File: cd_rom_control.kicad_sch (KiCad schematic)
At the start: 74 parts, among them IC103 CXD1167Q, IC104 D78C14GF, IC105 D6378GF, IC106 D4364G, P401 Conn_01x10, P404 Conn_01x08, P7 Conn_01x07, Q1 Q_NPN_CBE, Q102 Q_NPN_CBE, Q203 15 29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

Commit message: More passives on back.
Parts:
- added C138 (x5): ?, A-PCENGINE:SMD_0805_Narrow_Long, symbol Device:C
- added C138: ?, A-PCENGINE:SMD_0805_Narrow, symbol Device:C
- added R105: ?, A-PCENGINE:SMD_0805_Narrow, symbol Device:R
- added R105 (x19): ?, A-PCENGINE:SMD_0805_Narrow_Long, symbol Device:R
- added TP1 (x6), TP7 (x6): ~, A-PCENGINE:Test_Point_1.5mm, symbol Connector:TestPoint
- renumbered Q1 to Q105
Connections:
- net +5VD: now also C138.1, C138.1, C138.1, C138.1, C138.2, C138.2, TP1.1
- net ATSC: now also TP7.1
- net BCLK: now also R105.2
- net CIF4: now also R105.2
- net CIF5: now also R105.2
- net CIF6: now also R105.2
- net DA13: now also R105.1
- net DA14: now also R105.1
- net DA15: now also R105.1, R105.1
- net DA7: now also R105.1
- net DA8: now also R105.2
- net DATA: now also R105.2
- net FE: now also TP7.1
- net GND: now also C138.1, C138.1, C138.2, C138.2, C138.2, C138.2, R105.1, R105.1, R105.2
- net LRCK: now also R105.2
- net MD2: now also R105.2
- net P404P6: now also R105.2, R105.2
- net P7P5: now also TP7.1
- net P7P6: now also TP7.1
- net SCOR: now also R105.1
- net X0: now also R105.2
- net X1: now also R105.2, TP1.1
- net X2: now also R105.2
- net X3: now also R105.2, TP1.1
- net X4: now also R105.2
- net X5: now also R105.2, TP1.1
- net X6: now also R105.2, TP1.1
- net X7: now also R105.2, TP1.1
- net XCLK: now also TP7.1
- net at P3.1 (Pin_1): now also R105.1, TP7.1
- net at IC104.49: now also R105.1
- net at IC104.50: now also R105.1
- net at IC104.51: now also R105.1
- net at IC104.52: now also R105.1
- net at IC104.53: now also R105.1
- net at IC104.54: now also R105.1
- net at IC104.55: now also R105.1
- net at IC104.56: now also R105.1
- net at IC103.22 (SBSO): now also R105.1
- net at IC103.79 (WDCK): now also R105.2
- net at IC103.80 (LRCK): now also R105.1
- new net WCLK: R105.1
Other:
- moved on the sheet: C138, C951, P3, P401, P404, P7, Q102, R105, RA502

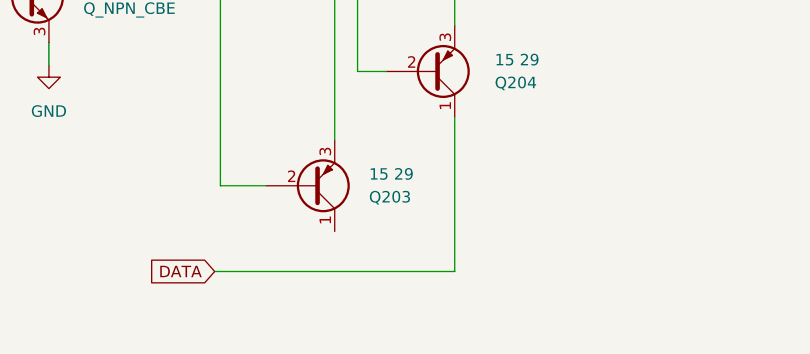
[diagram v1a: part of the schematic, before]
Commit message: Yet more passives on back.
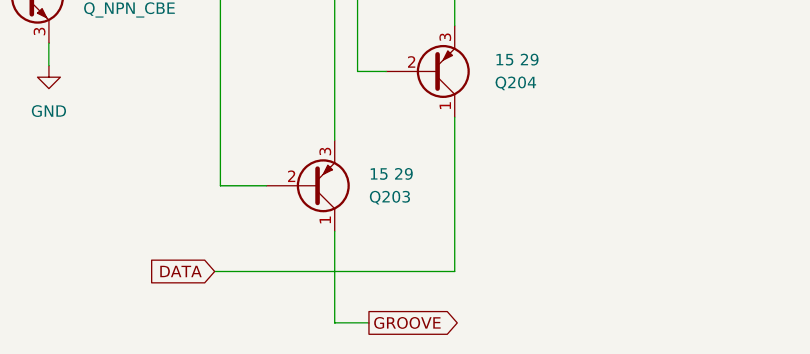
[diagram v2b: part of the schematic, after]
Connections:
- net GROOVE: now reaches Q203.1 (C)
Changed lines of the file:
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@@
+    (stroke (width 0) (type default))
+  )
+  (wire (pts (xy -20.32 314.96) (xy -20.32 325.12))
     (stroke (width 0) (type default))
   )
@@
   )
   (wire (pts (xy 220.98 269.24) (xy 220.98 273.685))
+    (stroke (width 0) (type default))
+  )
+  (wire (pts (xy -20.32 325.12) (xy -16.51 325.12))
     (stroke (width 0) (type default))
   )
@@
       (effects (font (size 1.27 1.27)) (justify left) hide)
     )
+  )
+  (global_label "GROOVE" (shape output) (at -16.51 325.12 0) (fields_autoplaced)
+    (effects (font (size 1.27 1.27)) (justify left))
+    (property "Intersheetrefs" "${INTERSHEET_REFS}" (at -6.0862 325.12 0)
+      (effects (font (size 1.27 1.27)) (justify left) hide)
+    )

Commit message: Fix DRC errors.
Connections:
- net DATA: no longer Q204.1 (C), R105.2
- net BW: now reaches Q102.1 (C), R105.2
- new net DATA2: Q204.1 (C), R105.2
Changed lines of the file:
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@@
   (junction (at -104.14 262.89) (diameter 0) (color 0 0 0 0)
   )
+  (junction (at 106.68 -31.115) (diameter 0) (color 0 0 0 0)
+  )
   (junction (at 121.285 29.845) (diameter 0) (color 0 0 0 0)
   )
@@
     (stroke (width 0) (type default))
   )
-  (wire (pts (xy -6.985 319.405) (xy -6.985 302.26))
+  (wire (pts (xy -6.985 307.848) (xy -6.985 302.26))
     (stroke (width 0) (type default))
   )
@@
     (stroke (width 0) (type default))
   )
+  (wire (pts (xy 106.68 -31.115) (xy 113.03 -31.115))
+    (stroke (width 0) (type default))
+  )
   (wire (pts (xy -44.45 220.98) (xy -114.3 220.98))
     (stroke (width 0) (type default))
@@
     (stroke (width 0) (type default))
   )
-  (wire (pts (xy -33.655 319.405) (xy -6.985 319.405))
+  (wire (pts (xy 0 307.848) (xy -6.985 307.848))
     (stroke (width 0) (type default))
   )
@@
     )
   )
-  (global_label "DATA" (shape input) (at 206.375 34.29 90) (fields_autoplaced)
+  (global_label "DATA2" (shape input) (at 206.375 34.29 90) (fields_autoplaced)
     (effects (font (size 1.27 1.27)) (justify left))
-    (property "Intersheetrefs" "${INTERSHEET_REFS}" (at 206.375 26.89 90)
+    (property "Intersheetrefs" "${INTERSHEET_REFS}" (at 206.375 25.6805 90)
       (effects (font (size 1.27 1.27)) (justify left) hide)
     )
@@
     )
   )
+  (global_label "BW" (shape input) (at 113.03 -31.115 0) (fields_autoplaced)
+    (effects (font (size 1.27 1.27)) (justify left))
+    (property "Intersheetrefs" "${INTERSHEET_REFS}" (at 118.7366 -31.115 0)
+      (effects (font (size 1.27 1.27)) (justify left) hide)
+    )
+  )
   (global_label "SCOR" (shape output) (at 121.285 21.59 90) (fields_autoplaced)
     (effects (font (size 1.27 1.27)) (justify left))
@@
     )
   )
-  (global_label "DATA" (shape input) (at -33.655 319.405 180) (fields_autoplaced)
-    (effects (font (size 1.27 1.27)) (justify right))
-    (property "Intersheetrefs" "${INTERSHEET_REFS}" (at -41.055 319.405 0)
-      (effects (font (size 1.27 1.27)) (justify right) hide)
+  (global_label "DATA2" (shape input) (at 0 307.848 0) (fields_autoplaced)
+    (effects (font (size 1.27 1.27)) (justify left))
+    (property "Intersheetrefs" "${INTERSHEET_REFS}" (at 8.6095 307.848 0)
+      (effects (font (size 1.27 1.27)) (justify left) hide)
     )
   )

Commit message: General clean-up.
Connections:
- net DA0: no longer names the net of IC103.62 (DA01)
- net DA1: no longer names the net of IC103.63 (DA02)
- net DA10: no longer names the net of IC103.72 (DA11), P404.7 (Pin_7)
- net DA11: no longer names the net of IC103.74 (DA12)
- net DA12: no longer names the net of IC103.75 (DA13)
- net DA13: no longer names the net of IC103.76 (DA14), R105.1
- net DA14: no longer names the net of IC103.77 (DA15), R105.1
- net DA15: no longer names the net of IC103.78 (DA16), R105.1, R105.1
- net DA2: no longer names the net of IC103.64 (DA03)
- net DA3: no longer names the net of IC103.65 (DA04)
- net DA4: no longer names the net of IC103.66 (DA05), P404.5 (Pin_5)
- net DA5: no longer names the net of IC103.67 (DA06)
- net DA6: no longer names the net of IC103.68 (DA07)
- net DA7: no longer names the net of IC103.69 (DA08), R105.1
- net DA8: no longer names the net of IC103.70 (DA09), R105.2
- net DA9: no longer names the net of IC103.71 (DA10)
- no-connect marks 15 -> 27
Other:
- moved on the sheet: P404, R105

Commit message: Add resistor values to schematics.
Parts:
- R105: value ? -> 2.2K
- R105: value ? -> 10K?
- R105: value ? -> 220
- R105: value ? -> 100K
- R105: value ? -> 1K
- R105: value ? -> 4.7K
- R105: value ? -> 3.3K
- R105: value ? -> 10K
- R105: value ? -> 47K
- R105: value ? -> 0

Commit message: Schematic clean-up.
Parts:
- removed IC104: D78C14GF, A-PCENGINE:QFP-64_19x13_Pitch1mm, symbol PC-Engine:D78C14GF
- added IC104: D78C14GF, A-PCENGINE:QFP-64_19x13_Pitch1mm, symbol PC-Engine:D78C14GF_Labeled
- P401: value Conn_01x10 -> ~
- P404: value Conn_01x08 -> ~
- Q102: value Q_NPN_CBE -> 24 30
- SW401: value SW_Push -> CD LID
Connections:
- net +5VD: now also IC104.36 (VAREF), IC104.37 (AVDD), IC104.57 (~{STOP}), IC104.58 (VDD), IC104.64 (PA5)
- net ACTIVE: now also IC104.63 (PA4)
- net CIF3: now also IC104.17 (PC6)
- net CRCF: now also IC104.62 (PA3)
- net DATA: now also IC104.19 (~{NMI})
- net FOK: now also IC104.18 (PC7)
- net GND: now also IC104.23 (MODE0), IC104.26 (VSS), IC104.27 (AVSS)
- net LID_A: now also IC104.8 (PB5)
- net MD2: now also IC104.3 (PB0)
- net MUTG: now also IC104.11 (PC0)
- net P3P4: now also IC104.35 (AN7)
- net SCOR: now also IC104.20 (INT1)
- net SENS: now also IC104.16 (PC5)
- net SQCK: now also IC104.13 (PC2)
- net SUBQ: now also IC104.12 (PC1)
- net XLT: now also IC104.6 (PB3)
- net XRST: now also IC104.2 (PA7)
- net at C138.2, R105.1, R105.2: now also IC104.33 (AN5)
- net at P402.4 (Pin_4), R105.1, TP4.1: now also IC104.10 (PB7)
- net at P402.3 (Pin_3), R105.1, TP3.1: now also IC104.9 (PB6)
- net at Q203.2 (B): now also IC104.4 (PB1)
- net at Q204.2 (B), TP7.1: now also IC104.7 (PB4)
- net at P402.7 (Pin_7), R105.1, TP7.1: now also IC104.34 (AN6)
- net at P402.9 (Pin_9), R105.1, TP6.1: now also IC104.32 (AN4)
- net at C138.1, CF101.1: now also IC104.25 (X1)
- net at R105.1: now also IC104.21 (MODE1)
- net at Q105.1 (C), R105.2: now also IC104.14 (PC3)
- net at C138.1, CF101.2: now also IC104.24 (X2)
- net at R105.1: now also IC104.52 (PD3)
- net at R105.1: now also IC104.51 (PD2)
- net at R105.1: now also IC104.56 (PD7)
- net at R105.1: now also IC104.55 (PD6)
- net at R105.1: now also IC104.50 (PD1)
- net at R105.1: now also IC104.54 (PD5)
- net at R105.1: now also IC104.49 (PD0)
- net at R105.1: now also IC104.53 (PD4)
- net DVCC renamed DCLK
- net DCLK: now also IC104.15 (PC4)
- net DX renamed ~{URESET}
- net ~{URESET}: now also IC104.22 (~{RESET})
- net KAK0 renamed UPA2
- net UPA2: now also IC104.61 (PA2)
- net KAK1 renamed UPA1
- net UPA1: now also IC104.60 (PA1)
- net KAK2 renamed UPA0
- net UPA0: now also IC104.59 (PA0)
- net KAK3 renamed UPC3
- net X0 renamed UPD7
- net X1 renamed UPD6
- net X2 renamed UPD5
- net X3 renamed UPD4
- net X4 renamed UPD3
- net X5 renamed UPD2
- net X6 renamed UPD1
- net X7 renamed UPD0
- net Y0 renamed UPF5
- net UPF5: now also IC104.46 (PF5)
- net Y1 renamed UPF4
- net UPF4: now also IC104.45 (PF4)
- net Y2 renamed UPF3
- net UPF3: now also IC104.44 (PF3)
- net Y3 renamed UPF2
- net UPF2: now also IC104.43 (PF2)
- net Y4 renamed UPF1
- net UPF1: now also IC104.42 (PF1)
- net Y5 renamed UPF0
- net UPF0: now also IC104.41 (PF0)
- net Y6 renamed UALE
- net UALE: now also IC104.40 (ALE)
- net Y7 renamed ~{UWR}
- net ~{UWR}: now also IC104.39 (~{WR})
- net Y8 renamed ~{URD}
- net ~{URD}: now also IC104.38 (~{RD})
- no-connect marks 27 -> 30
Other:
- moved on the sheet: C105, C138, C951, CF101, D102, IC103, IC105, IC106, L106, P3, P401, P402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

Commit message: Intermediate commit after renaming some nets.
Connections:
- net CFX10 is gone; now on net CFX0: IC105.46
- net CFX8 is gone; now on net CFX2: IC105.44
- net CFX9 is gone; now on net CFX1: IC105.45
- net CFX0: no longer R105.1
- net CFX1: no longer R105.1
- net CFX2: no longer R105.1
- net CFX3: now also IC105.43; no longer IC105.38
- net CFX4: now also IC105.42; no longer IC105.39
- net CFX6: now also IC105.39; no longer IC105.42
- net CFX7: now also IC105.38; no longer IC105.43
- net COE renamed ~{COE}
- net CWE renamed ~{CWE}
- new net CFS0: R105.1
- new net CFS1: R105.1
- new net CFS2: R105.1
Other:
- moved on the sheet: C138, C951, IC106, L106
